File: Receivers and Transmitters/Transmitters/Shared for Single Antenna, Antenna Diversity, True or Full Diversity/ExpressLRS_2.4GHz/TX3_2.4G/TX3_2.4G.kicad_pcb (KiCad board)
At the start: 4 copper layers, 39.8 x 55.8 mm, 34 parts, among them J1 Conn_01x05_Socket, J2 Conn_01x03_Socket, J3 Conn_01x04_Socket, J4 Conn_02x06_Odd_Even, U1 TPS7A4701xRGW, U2 ESP32-WROOM-32, U3 E28-2G4M27S, U4 ESP8285H16, Y2 26MHz

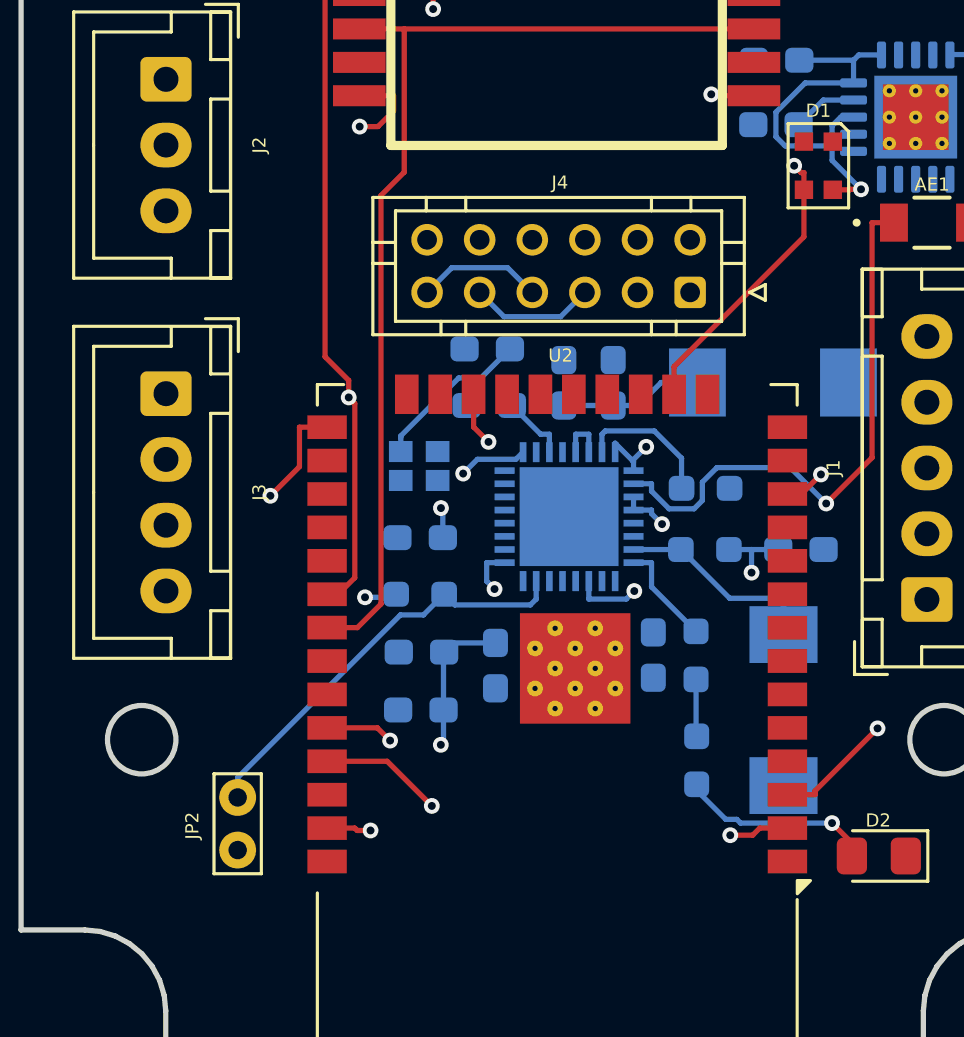
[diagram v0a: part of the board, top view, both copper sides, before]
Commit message: Fixed incorrect LED RGB connection to ESP32 on TX2_2.4G and TX3_2.4G schematics and PCBs
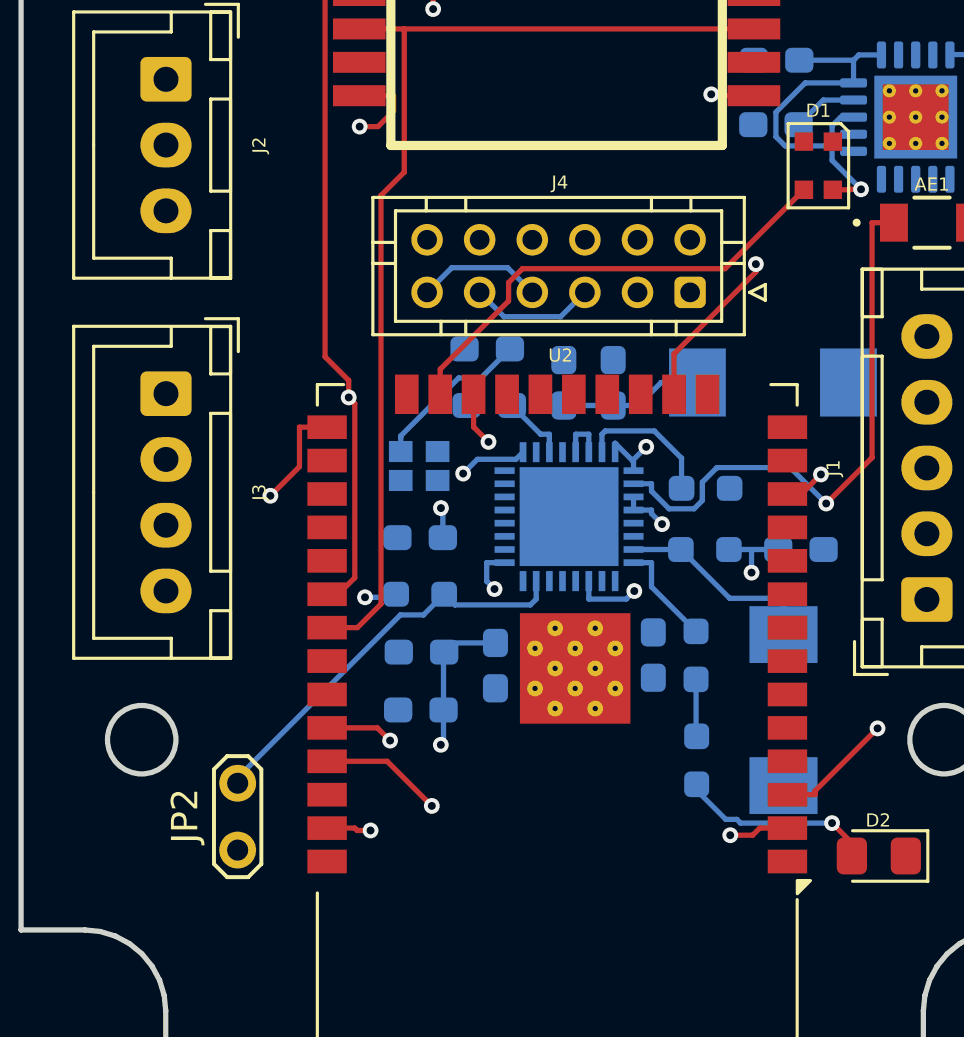
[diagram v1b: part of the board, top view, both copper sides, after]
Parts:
- JP2: footprint TestPoint:TestPoint_Bridge_Pitch2.0mm_Drill0.7mm -> TestPoint:TestPoint_2Pads_Pitch2.54mm_Drill0.8mm
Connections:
- D1 pad 3: /SPORT -> /LED_RGB
- U2 pad 23: unconnected-(U2-IO15-Pad23) -> /LED_RGB
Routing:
- net /LED_RGB: track 0.00 -> 18.0 mm
- net /SPORT: track 36.2 -> 33.4 mm
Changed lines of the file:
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@@
 			(psa4output no)
 			(plot_black_and_white yes)
-			(plotinvisibletext no)
 			(sketchpadsonfab no)
 			(plotpadnumbers no)
@@
 	(net 40 "unconnected-(U2-IO17-Pad28)")
 	(net 41 "/NRESET")
-	(net 42 "unconnected-(U2-IO15-Pad23)")
+	(net 42 "/LED_RGB")
 	(net 43 "unconnected-(U2-NC-Pad32)")
 	(net 44 "/DIO1")
@@
 			(size 0.7 0.7)
 			(layers "F.Cu" "F.Mask" "F.Paste")
-			(net 6 "/SPORT")
+			(net 42 "/LED_RGB")
 			(pinfunction "DIN")
 			(pintype "input")
@@
 		)
 	)
-	(footprint "TestPoint:TestPoint_Bridge_Pitch2.0mm_Drill0.7mm"
+	(footprint "TestPoint:TestPoint_2Pads_Pitch2.54mm_Drill0.8mm"
 		(layer "F.Cu")
 		(at 137.325 103.475 90)
-		(descr "wire loop as test point, pitch 2.0mm, hole diameter 0.7mm, wire diameter 0.5mm")
-		(tags "test point wire loop")
+		(descr "Test point with 2 pins, pitch 2.54mm, drill diameter 0.8mm")
+		(tags "CONN DEV")
 		(property "Reference" "JP2"
-			(at 0.925 -1.725 90)
+			(at 1.3 -2 90)
 			(layer "F.SilkS")
 			(effects
 				(font
-					(size 0.5 0.5)
-					(thickness 0.08)
+					(size 1 1)
+					(thickness 0.15)
 				)
 			)
 		)
 		(property "Value" "Jumper_2_Small_Bridged"
-			(at 1 -1.7 90)
+			(at 1.27 2 90)
 			(layer "F.Fab")
-			(hide yes)
 			(effects
 				(font
@@
 		(sheetname "/ESP8285/")
 		(sheetfile "ESP8285.kicad_sch")
-		(attr through_hole)
+		(attr exclude_from_pos_files)
 		(fp_line
-			(start 2.9 -0.9)
-			(end -0.9 -0.9)
+			(start 3.07 -0.9)
+			(end 3.57 -0.4)
 			(stroke
-				(width 0.12)
+				(width 0.15)
 				(type solid)
 			)
@@
 		)
 		(fp_line
-			(start -0.9 -0.9)
-			(end -0.9 0.9)
+			(start -0.53 -0.9)
+			(end 3.07 -0.9)
 			(stroke
-				(width 0.12)
+				(width 0.15)
 				(type solid)
 			)
@@
 		)
 		(fp_line
-			(start 2.9 0.9)
-			(end 2.9 -0.9)
+			(start 3.57 -0.4)
+			(end 3.57 0.4)
 			(stroke
-				(width 0.12)
+				(width 0.15)
 				(type solid)
 			)
@@
 		)
 		(fp_line
-			(start -0.9 0.9)
-			(end 2.9 0.9)
+			(start -1.03 -0.4)
+			(end -0.53 -0.9)
 			(stroke
-				(width 0.12)
+				(width 0.15)
+				(type solid)
+			)
+			(layer "F.SilkS")
+		)
+		(fp_line
+			(start 3.57 0.4)
+			(end 3.07 0.9)
+			(stroke
+				(width 0.15)
 				(type solid)
 			)
@@
 		)
 		(fp_line
-			(start 3.2 -1.2)
-			(end -1.2 -1.2)
+			(start -1.03 0.4)
+			(end -1.03 -0.4)
+			(stroke
+				(width 0.15)
+				(type solid)
+			)
+			(layer "F.SilkS")
+		)
+		(fp_line
+			(start 3.07 0.9)
+			(end -0.53 0.9)
+			(stroke
+				(width 0.15)
+				(type solid)
+			)
+			(layer "F.SilkS")
+		)
+		(fp_line
+			(start -0.53 0.9)
+			(end -1.03 0.4)
+			(stroke
+				(width 0.15)
+				(type solid)
+			)
+			(layer "F.SilkS")
+		)
+		(fp_line
+			(start 3.15 -1.15)
+			(end -0.65 -1.15)
 			(stroke
 				(width 0.05)
@@
 		)
 		(fp_line
-			(start 3.2 -1.2)
-			(end 3.2 1.2)
+			(start -0.65 -1.15)
+			(end -1.3 -0.5)
 			(stroke
 				(width 0.05)
@@
 		)
 		(fp_line
-			(start -1.2 1.2)
-			(end -1.2 -1.2)
+			(start 3.8 -0.5)
+			(end 3.15 -1.15)
 			(stroke
 				(width 0.05)
@@
 		)
 		(fp_line
-			(start -1.2 1.2)
-			(end 3.2 1.2)
+			(start -1.3 -0.5)
+			(end -1.3 0.5)
 			(stroke
 				(width 0.05)
@@
 		)
 		(fp_line
-			(start 2 0)
-			(end 0 0)
+			(start 3.8 0.5)
+			(end 3.8 -0.5)
 			(stroke
-				(width 0.12)
+				(width 0.05)
+				(type solid)
+			)
+			(layer "F.CrtYd")
+		)
+		(fp_line
+			(start -1.3 0.5)
+			(end -0.65 1.15)
+			(stroke
+				(width 0.05)
+				(type solid)
+			)
+			(layer "F.CrtYd")
+		)
+		(fp_line
+			(start 3.15 1.15)
+			(end 3.8 0.5)
+			(stroke
+				(width 0.05)
+				(type solid)
+			)
+			(layer "F.CrtYd")
+		)
+		(fp_line
+			(start -0.65 1.15)
+			(end 3.15 1.15)
+			(stroke
+				(width 0.05)
 				(type solid)
 			)
+			(layer "F.CrtYd")
+		)
+		(fp_text user "${REFERENCE}"
+			(at 1.3 -2 90)
 			(layer "F.Fab")
+			(effects
+				(font
+					(size 1 1)
+					(thickness 0.15)
+				)
+			)
 		)
 		(pad "1" thru_hole circle
 			(at 0 0 90)
 			(size 1.4 1.4)
-			(drill 0.7)
+			(drill 0.8)
 			(layers "*.Cu" "*.Mask")
 			(remove_unused_layers no)
@@
 			(pintype "passive")
 		)
-		(pad "1" thru_hole circle
-			(at 2 0 90)
+		(pad "2" thru_hole circle
+			(at 2.54 0 90)
 			(size 1.4 1.4)
-			(drill 0.7)
+			(drill 0.8)
 			(layers "*.Cu" "*.Mask")
 			(remove_unused_layers no)
-			(net 55 "Net-(JP2-A)")
-			(pinfunction "A")
+			(net 1 "GND")
+			(pinfunction "B")
 			(pintype "passive")
 		)
 		(embedded_fonts no)
-		(model "${KICAD9_3DMODEL_DIR}/Connector_PinHeader_2.00mm.3dshapes/PinHeader_1x02_P2.00mm_Vertical.step"
-			(offset
-				(xyz 0 0 0)
-			)
-			(scale
-				(xyz 1 1 1)
-			)
-			(rotate
-				(xyz -0 -0 -90)
-			)
-		)
 	)
 	(footprint "Connector_JST:JST_XH_B3B-XH-A_1x03_P2.50mm_Vertical"
@@
 			(size 1.5 0.9)
 			(layers "F.Cu" "F.Mask" "F.Paste")
-			(net 42 "unconnected-(U2-IO15-Pad23)")
+			(net 42 "/LED_RGB")
 			(pinfunction "IO15")
-			(pintype "bidirectional+no_connect")
+			(pintype "bidirectional")
 		)
 		(pad "24" smd rect
@@
 	)
 	(segment
-		(start 158.85 78.375)
-		(end 158.85 77.7233)
+		(start 157.025 81.2)
+		(end 157.025 81.5)
 		(width 0.2)
 		(layer "F.Cu")
@@
 	)
 	(segment
-		(start 153.915 86.15)
-		(end 153.915 85.0983)
+		(start 157.025 81.5)
+		(end 153.915 84.61)
 		(width 0.2)
 		(layer "F.Cu")
@@
 	)
 	(segment
-		(start 158.7436 77.7233)
-		(end 158.85 77.7233)
+		(start 153.915 84.61)
+		(end 153.915 86.15)
 		(width 0.2)
 		(layer "F.Cu")
 		(net 6)
 	)
-	(segment
-		(start 158.4803 77.46)
-		(end 158.7436 77.7233)
-		(width 0.2)
-		(layer "F.Cu")
+	(via
+		(at 157.025 81.2)
+		(size 0.6)
+		(drill 0.3)
+		(layers "F.Cu" "B.Cu")
 		(net 6)
 	)
 	(segment
-		(start 158.85 80.1633)
-		(end 158.85 78.375)
+		(start 157.025 81.2)
+		(end 157.025 78.15)
 		(width 0.2)
-		(layer "F.Cu")
+		(layer "In1.Cu")
 		(net 6)
 	)
 	(segment
-		(start 153.915 85.0983)
-		(end 158.85 80.1633)
+		(start 156.335 77.46)
+		(end 137.885 77.46)
 		(width 0.2)
-		(layer "F.Cu")
-		(net 6)
-	)
-	(via
-		(at 158.4803 77.46)
-		(size 0.6)
-		(drill 0.3)
-		(layers "F.Cu" "B.Cu")
+		(layer "In1.Cu")
 		(net 6)
 	)
 	(segment
-		(start 134.6 74.175)
-		(end 137.885 77.46)
+		(start 157.025 78.15)
+		(end 156.335 77.46)
 		(width 0.2)
 		(layer "In1.Cu")
@@
 	(segment
 		(start 137.885 77.46)
-		(end 158.4803 77.46)
+		(end 134.6 74.175)
 		(width 0.2)
 		(layer "In1.Cu")
@@
 	)
 	(segment
+		(start 155.851 81.374)
+		(end 148.151793 81.374)
+		(width 0.2)
+		(layer "F.Cu")
+		(net 42)
+	)
+	(segment
+		(start 145.025 85.2)
+		(end 145.025 86.15)
+		(width 0.2)
+		(layer "F.Cu")
+		(net 42)
+	)
+	(segment
+		(start 147.624 81.901793)
+		(end 147.624 82.601)
+		(width 0.2)
+		(layer "F.Cu")
+		(net 42)
+	)
+	(segment
+		(start 147.624 82.601)
+		(end 145.025 85.2)
+		(width 0.2)
+		(layer "F.Cu")
+		(net 42)
+	)
+	(segment
+		(start 158.85 78.375)
+		(end 155.851 81.374)
+		(width 0.2)
+		(layer "F.Cu")
+		(net 42)
+	)
+	(segment
+		(start 148.151793 81.374)
+		(end 147.624 81.901793)
+		(width 0.2)
+		(layer "F.Cu")
+		(net 42)
+	)
+	(segment
